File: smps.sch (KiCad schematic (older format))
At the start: 152 parts, among them J1 AC, J2 OUT0, J3 OUT1, Q1 TBD, Q2 STF7N80K5, Q3 2N5551, Q4 STF7N80K5, Q5 2N5551, Q6 TBD, Q7 2N5551, U1 MAX4080S, U10 AMS1117-3.3, U3 LMV324, U4 MAX4080S, U5 STCH03TR, U6 PC817X2, U7 STCH03TR, U8 SFH617A-2, U9 XL7005A

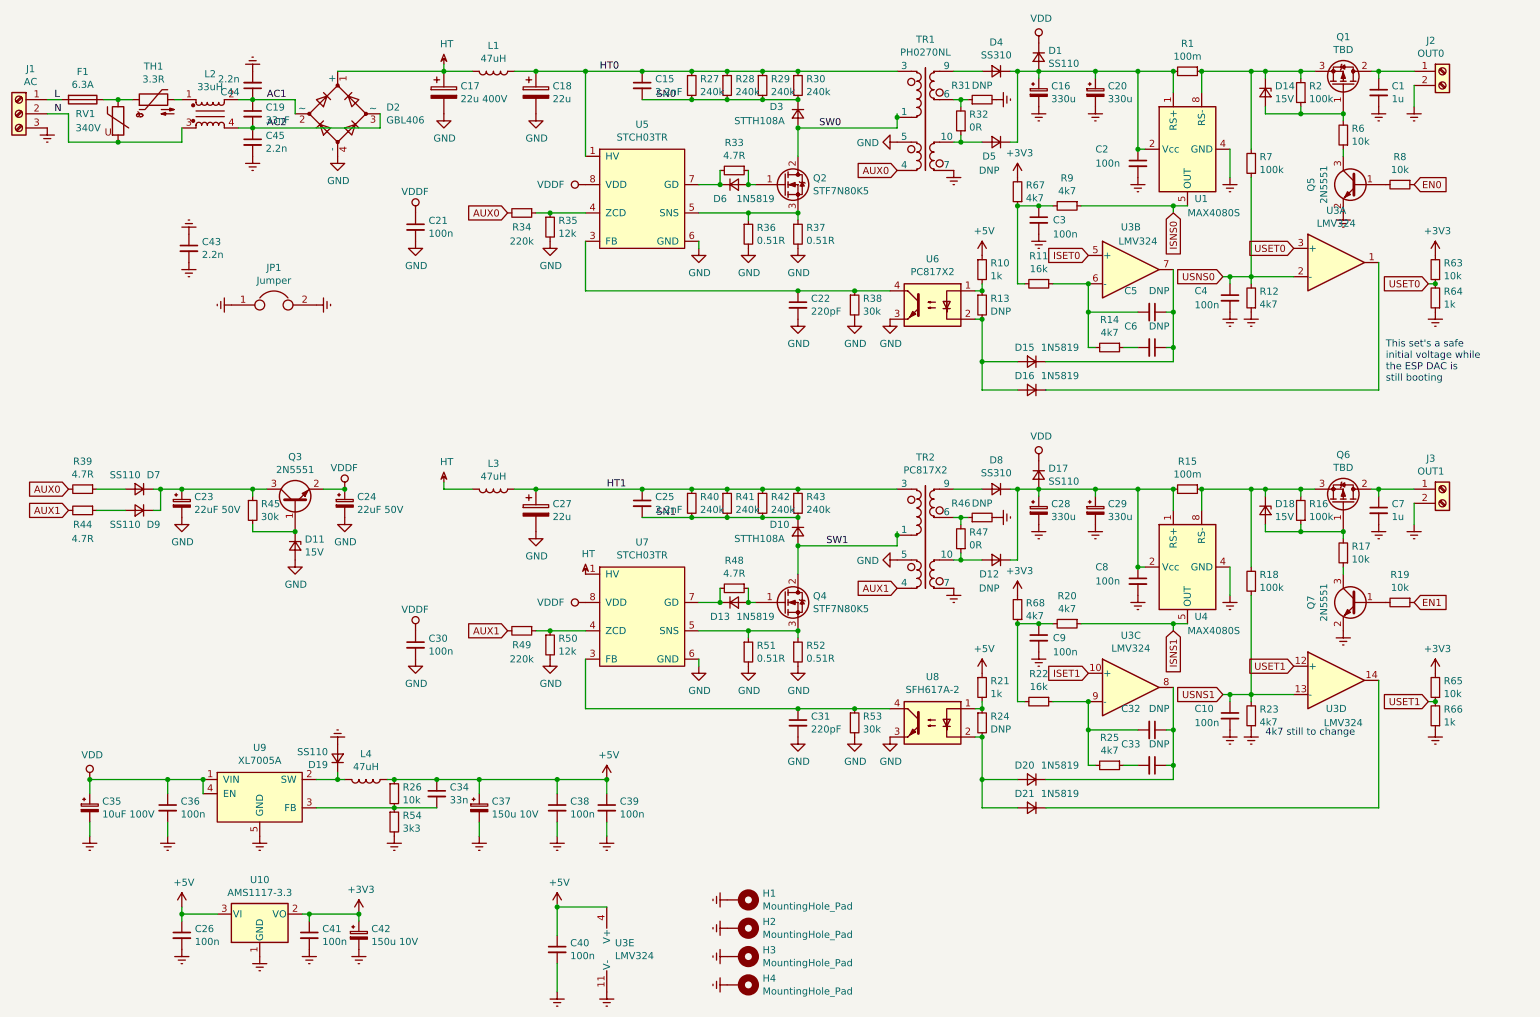
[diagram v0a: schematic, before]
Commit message: fixed some schematic values
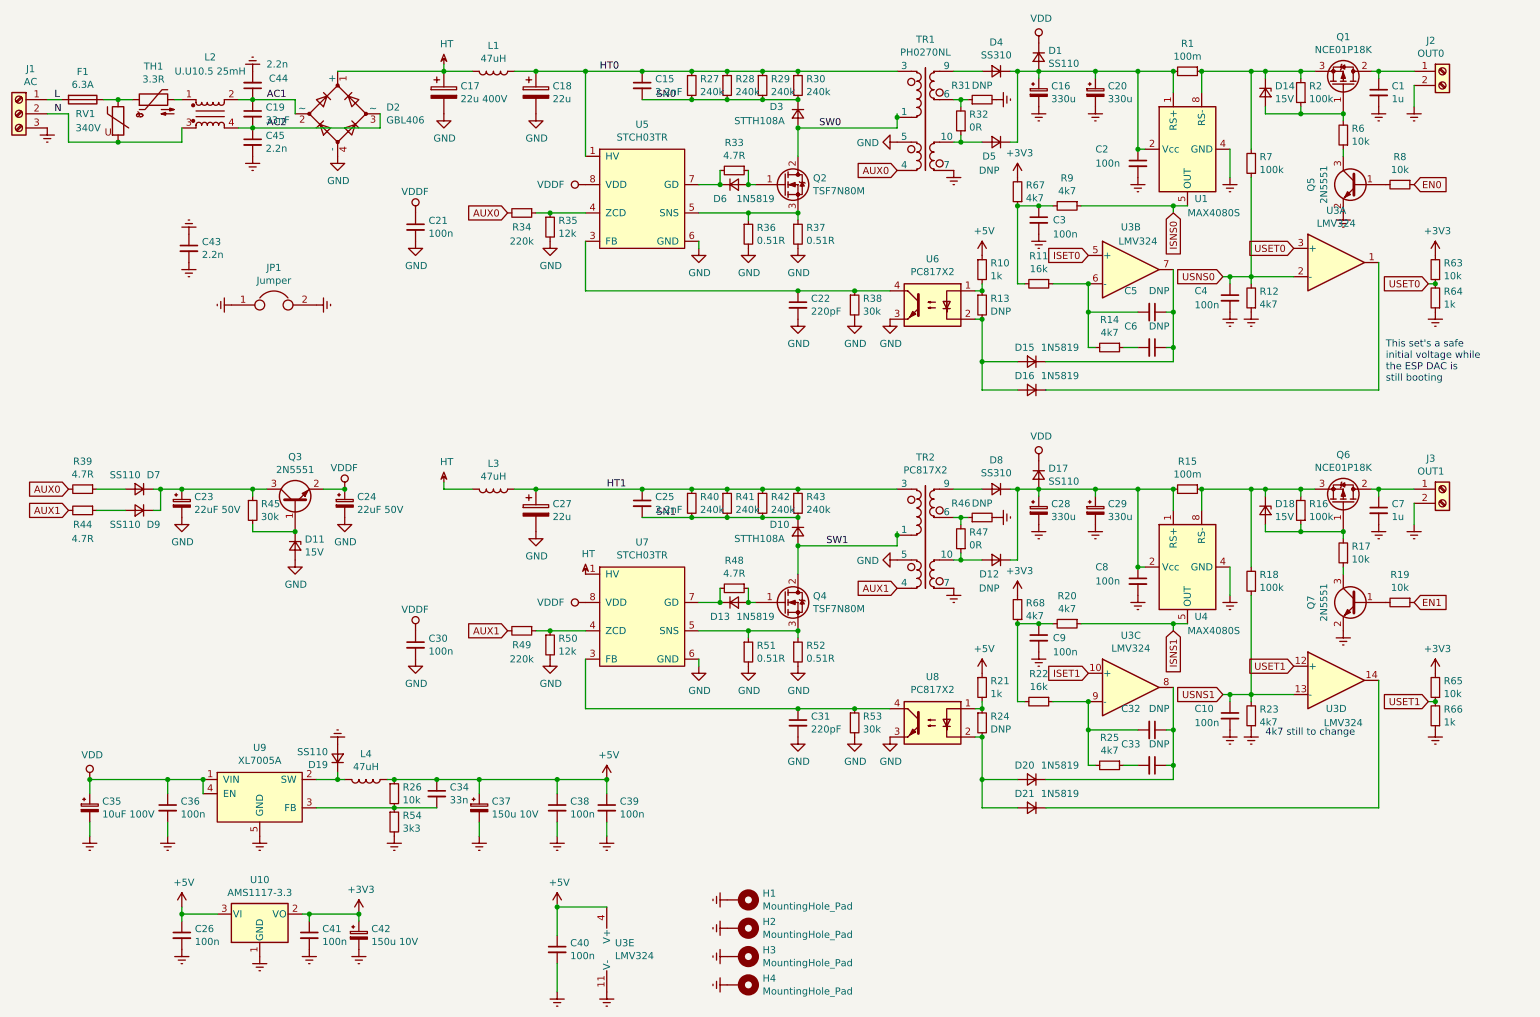
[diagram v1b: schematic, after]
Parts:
- L2: value 33uH -> U.U10.5 25mH
- Q1, Q6: value TBD -> NCE01P18K
- Q2, Q4: value STF7N80K5 -> TSF7N80M
- U8: value SFH617A-2 -> PC817X2
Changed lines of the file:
@@
 P 6100 1750
 F 0 "Q2" H 6306 1796 50  0000 L CNN
-F 1 "STF7N80K5" H 6306 1705 50  0000 L CNN
+F 1 "TSF7N80M" H 6306 1705 50  0000 L CNN
 F 2 "Package_TO_SOT_THT:TO-220-3_Vertical" H 6300 1850 50  0001 C CNN
 F 3 "~" H 6100 1750 50  0001 C CNN
@@
 U 1 1 5E6E6042
 P 2050 1250
-F 0 "L2" H 2050 1531 50  0000 C CNN
-F 1 "33uH" H 2050 1440 50  0000 C CNN
+F 0 "L2" H 2050 1650 50  0000 C CNN
+F 1 "U.U10.5 25mH" H 2050 1550 50  0000 C CNN
 F 2 "libs:L_CommonMode_U.U_multi" H 2050 1250 50  0001 C CNN
 F 3 "~" H 2050 1250 50  0001 C CNN
@@
 P 6100 4700
 F 0 "Q4" H 6306 4746 50  0000 L CNN
-F 1 "STF7N80K5" H 6306 4655 50  0000 L CNN
+F 1 "TSF7N80M" H 6306 4655 50  0000 L CNN
 F 2 "Package_TO_SOT_THT:TO-220-3_Vertical" H 6300 4800 50  0001 C CNN
 F 3 "~" H 6100 4700 50  0001 C CNN
@@
 P 7150 5550
 F 0 "U8" H 7150 5875 50  0000 C CNN
-F 1 "SFH617A-2" H 7150 5784 50  0000 C CNN
+F 1 "PC817X2" H 7150 5784 50  0000 C CNN
 F 2 "Package_DIP:DIP-4_W7.62mm" H 6950 5350 50  0001 L CIN
 F 3 "http://www.vishay.com/docs/83740/sfh617a.pdf" H 7150 5550 50  0001 L CNN
@@
 	1    0    0    -1
 $EndComp
-$Comp
-L Device:Q_PMOS_GDS Q1
-U 1 1 5EBA3176
-P 10050 1050
-F 0 "Q1" V 10393 1050 50  0000 C CNN
-F 1 "TBD" V 10302 1050 50  0000 C CNN
-F 2 "Package_TO_SOT_SMD:TO-252-2" H 10250 1150 50  0001 C CNN
-F 3 "~" H 10050 1050 50  0001 C CNN
-	1    10050 1050
-	0    1    -1   0
-$EndComp
 Connection ~ 9050 950
 $Comp
@@
 P 10050 4000
 F 0 "Q6" V 10393 4000 50  0000 C CNN
-F 1 "TBD" V 10302 4000 50  0000 C CNN
+F 1 "NCE01P18K" V 10302 4000 50  0000 C CNN
 F 2 "Package_TO_SOT_SMD:TO-252-2" H 10250 4100 50  0001 C CNN
 F 3 "~" H 10050 4000 50  0001 C CNN
@@
 U 1 1 5FF05D0B
 P 2350 1050
-F 0 "C44" H 2442 1096 50  0000 L CNN
-F 1 "2.2n" H 2442 1005 50  0000 L CNN
+F 0 "C44" H 2100 1000 50  0000 L CNN
+F 1 "2.2n" H 2100 900 50  0000 L CNN
 F 2 "Varistor:RV_Disc_D9mm_W4mm_P5mm" H 2350 1050 50  0001 C CNN
 F 3 "~" H 2350 1050 50  0001 C CNN
@@
 	7750 1900 7750 2450
 Connection ~ 7750 1900
+$Comp
+L Device:Q_PMOS_GDS Q1
+U 1 1 5EBA3176
+P 10050 1050
+F 0 "Q1" V 10393 1050 50  0000 C CNN
+F 1 "NCE01P18K" V 10302 1050 50  0000 C CNN
+F 2 "Package_TO_SOT_SMD:TO-252-2" H 10250 1150 50  0001 C CNN
+F 3 "~" H 10050 1050 50  0001 C CNN
+	1    10050 1050
+	0    1    -1   0
+$EndComp
 $EndSCHEMATC

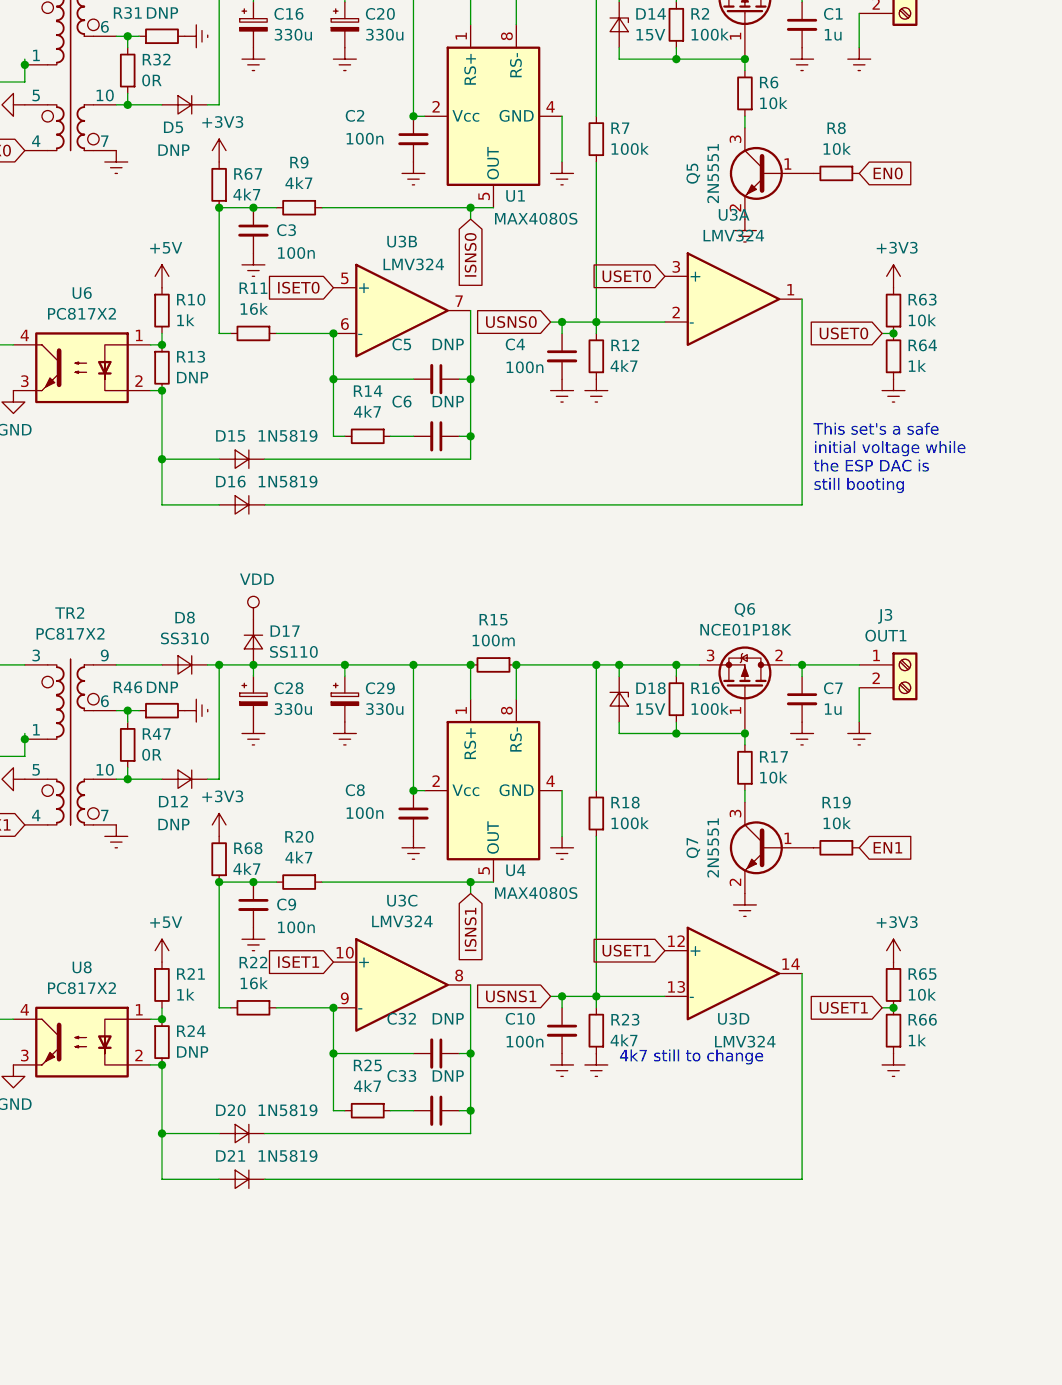
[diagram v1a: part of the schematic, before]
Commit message: modified Voltage DAC bias
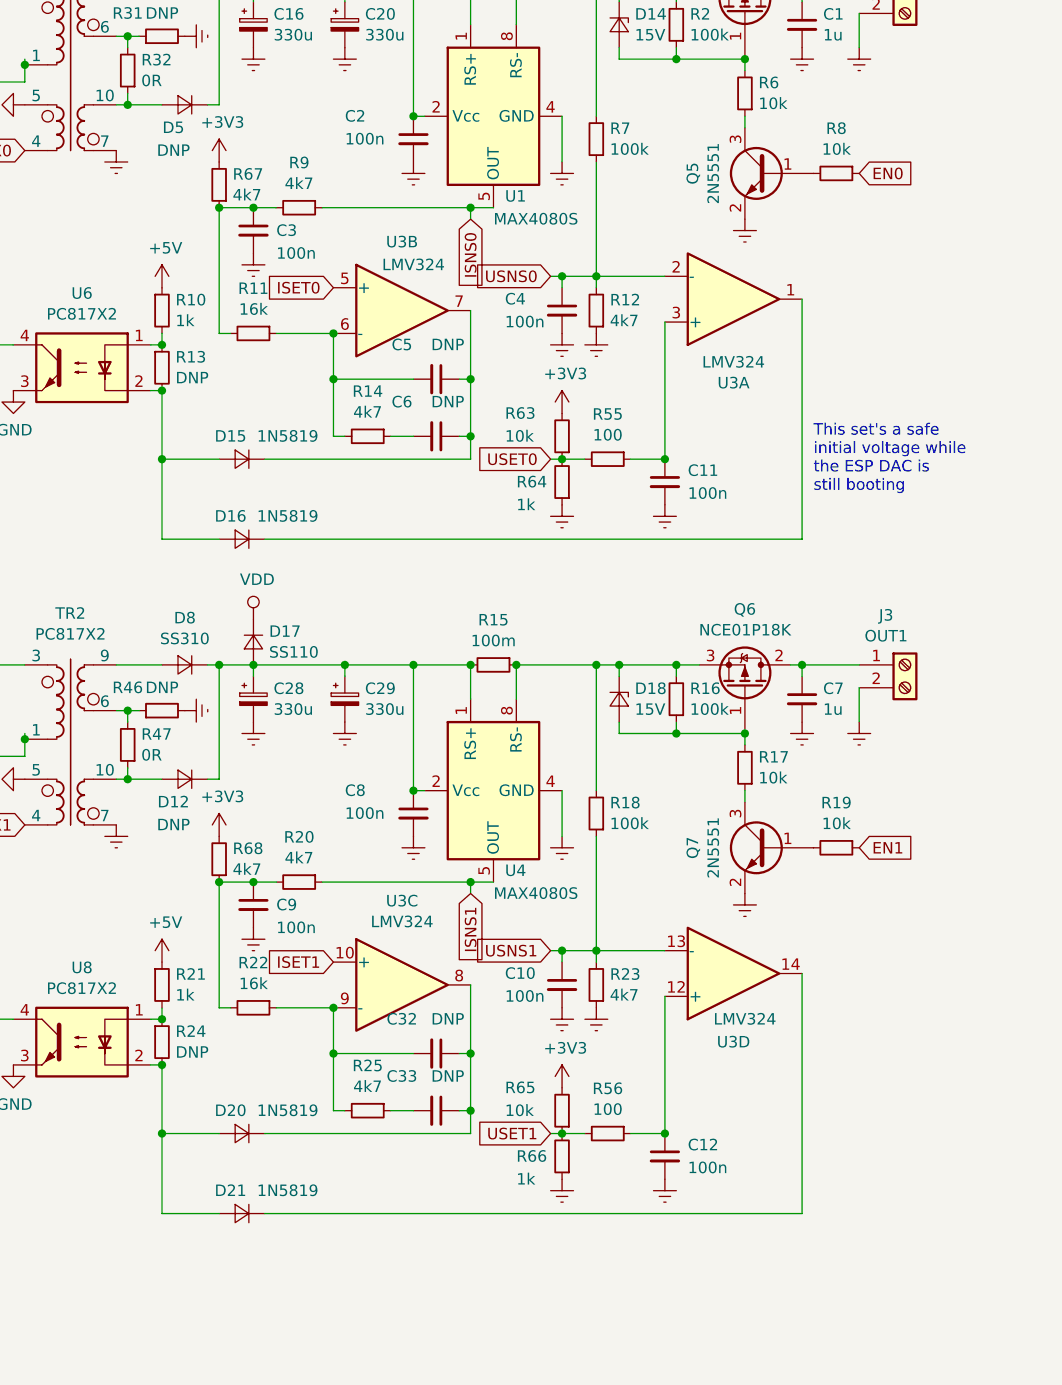
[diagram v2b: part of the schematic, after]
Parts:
- added C11, C12: 100n, Capacitor_SMD:C_0603_1608Metric, symbol Device:C_Small
- added R55, R56: 100, Resistor_SMD:R_0603_1608Metric, symbol Device:R_Small
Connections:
- net Earth: now also C11.2, C12.2
- net USET0: now also R55.2; no longer U3.3 (+)
- net USET1: now also R56.2; no longer U3.12 (+)
- new net: C11.1, R55.1, U3.3 (+)
- new net: C12.1, R56.1, U3.12 (+)
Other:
- note removed: "4k7 still to change"
- moved on the sheet: C10, C4, D16, D21, R12, R23, R63, R64
